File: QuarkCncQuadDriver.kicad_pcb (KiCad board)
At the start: 4 copper layers, 100 x 100 mm, 182 parts, among them J1 Screw_Terminal_01x02, J10 Screw_Terminal_01x02, J11 Screw_Terminal_01x04, J12 Screw_Terminal_01x04, J13 Screw_Terminal_01x04, J14 Conn_01x02_Male, J2 Conn_01x03_Male, J3 USB_B_Micro, J4 Screw_Terminal_01x02, J5 Screw_Terminal_01x02, J6 Conn_02x04_Odd_Even, J7 Conn_02x04_Odd_Even, J8 Conn_02x04_Odd_Even, J9 Conn_02x04_Odd_Even, Q1 WSF50P10, SW1 SW_DIP_x01, SW2 SW_DIP_x01, SW3 SW_DIP_x04, U1 StepperDriver_Conn2, U10 EL357N-G, U11 EL357N-G, U12 EL0631(TA), U13 EL357N-G, U14 EL357N-G, U15 EL0631(TA), U16 EL357N-G, U17 EL357N-G, U18 EL0631(TA), U19 StepperDriver_Conn2, U2 StepperDriver, U20 StepperDriver, U21 StepperDriver_Conn1, U22 W25Q128JVS, U23 RP2040, U24 tps54331DR, U25 LM5576, U26 SP3485EN-L/TR, U27 StepperDriver_Conn2, U28 StepperDriver, U29 StepperDriver_Conn1, U3 StepperDriver_Conn1, U4 EL357N-G, U5 EL357N-G, U6 EL0631(TA), U7 StepperDriver_Conn2, U8 StepperDriver, U9 StepperDriver_Conn1, Y1 X322512MSB4SI

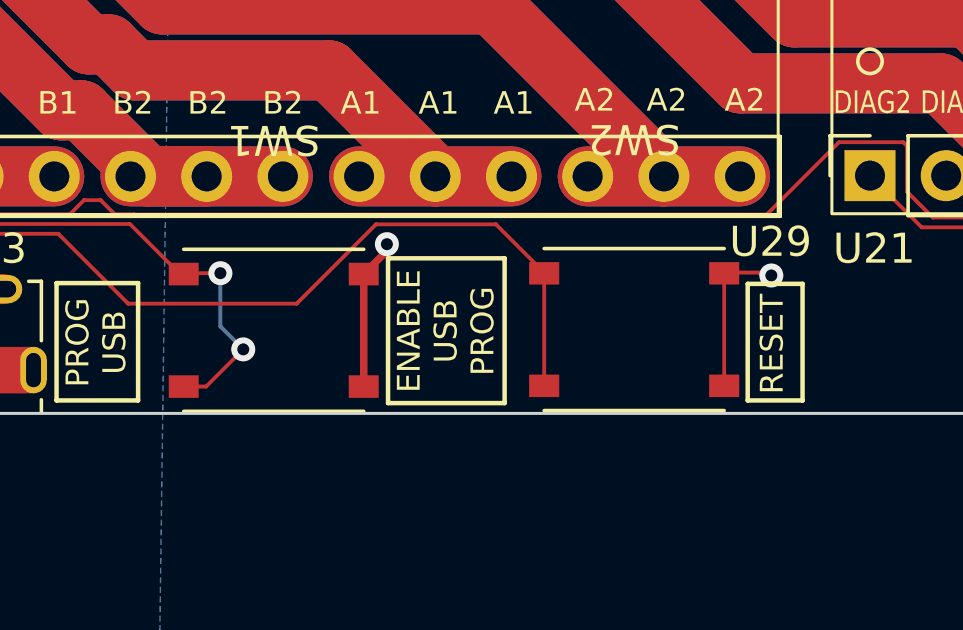
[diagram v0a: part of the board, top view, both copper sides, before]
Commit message: Fixed reset/boot button footprint
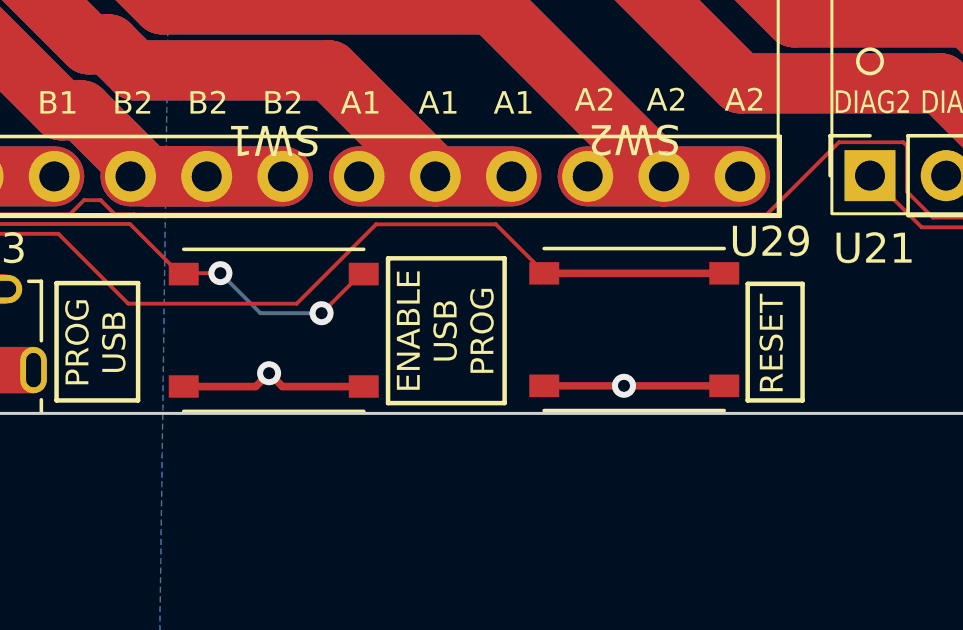
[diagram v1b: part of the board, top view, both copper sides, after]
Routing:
- net /RP2040 Microcontroller/RUN: track 141.0 -> 143.3 mm
- net GND: track 89.4 -> 91.3 mm
- net /RP2040 Microcontroller/~{USB_BOOT}: track 89.0 -> 89.6 mm

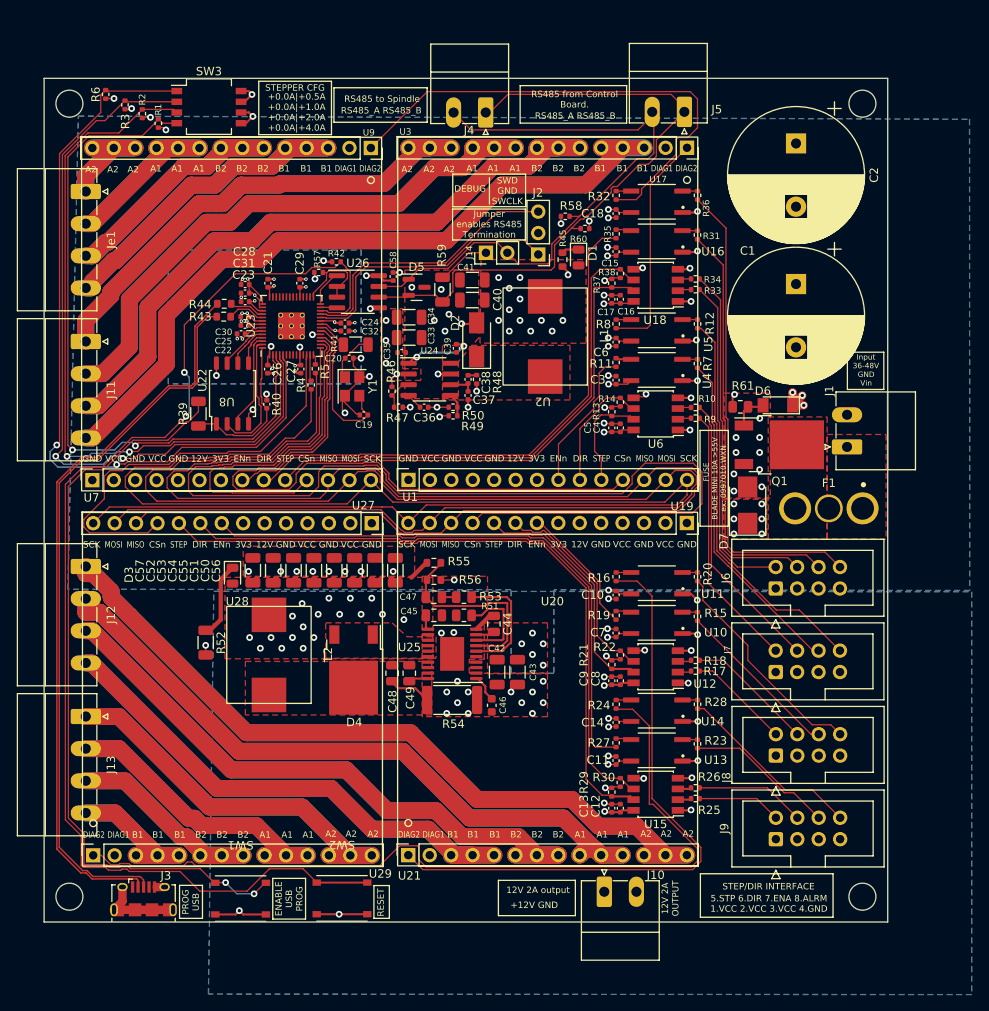
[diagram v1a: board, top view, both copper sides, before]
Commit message: Keyed stepper drivers. Larger input connector
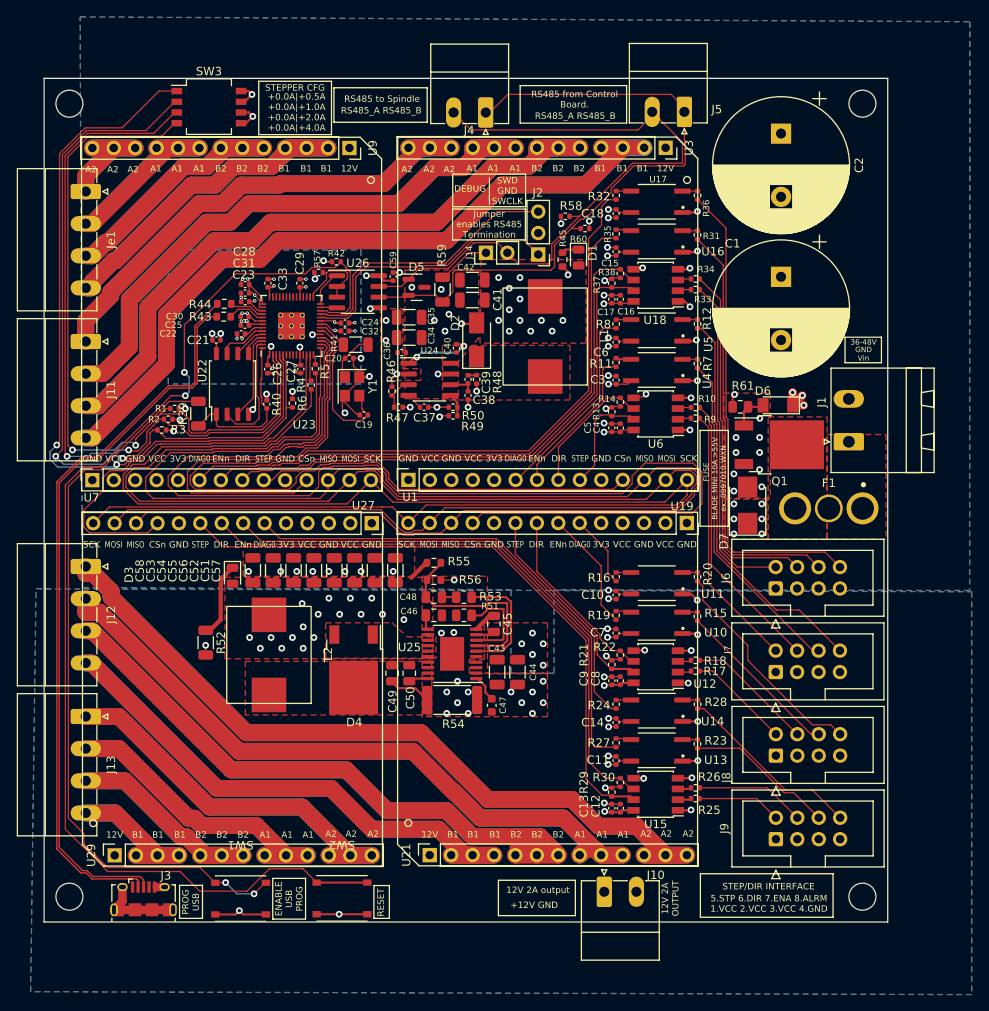
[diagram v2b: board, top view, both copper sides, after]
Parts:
- added C33: 100n 50V, Capacitor_SMD:C_0402_1005Metric, F.Cu at (63.9, 55.4)
- J1: footprint Connector_Phoenix_MC:PhoenixContact_MC_1,5_2-G-3.81_1x02_P3.81mm_Horizontal -> Connector_Phoenix_MSTB:PhoenixContact_MSTBA_2,5_2-G-5,08_1x02_P5.08mm_Horizontal
- U2, U20, U28, U8: footprint QuarkCncQuadDriver:StepperDriverV2 -> QuarkCncQuadDriver:StepperDriverV3
- U21, U29, U3, U9: footprint Connector_PinSocket_2.54mm:PinSocket_1x14_P2.54mm_Vertical -> Connector_PinSocket_2.54mm:PinSocket_1x13_P2.54mm_Vertical
- moved R6 42.8 mm to (66.8, 69.6), turned to -90 degrees
- moved R3 38.8 mm to (51.3, 72.8), turned to 180 degrees
- moved R2 36.3 mm to (52.1, 71.5), turned to 180 degrees
- moved R1 33.9 mm to (52.8, 70.2), turned to 180 degrees
- moved C21 9.08 mm to (57.8, 62.1), turned to 0 degrees
- moved U9 2.54 mm to (73.6, 39.3)
- moved U29 2.54 mm to (45.7, 123.2)
- moved U3 2.54 mm to (111.0, 39.3)
- moved U21 2.54 mm to (83.1, 123.2)
- moved C2 2.13 mm to (124.7, 37.6)
- moved C1 1.98 mm to (124.7, 54.6)
- moved U22 1.14 mm to (59.7, 67.3)
- moved J1 0.64 mm to (132.7, 74.2)
- renumbered C33 to C34, C34 to C35, C35 to C36, C36 to C37, C37 to C38, C38 to C39, C39 to C40, C40 to C41, C41 to C42, C42 to C43, C43 to C44, C44 to C45, C45 to C46, C46 to C47, C47 to C48, C48 to C49, C49 to C50, C50 to C51, C51 to C52, C52 to C53, C53 to C54, C54 to C55, C55 to C56, C56 to C57, C57 to C58, C58 to C59
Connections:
- U1 pad 10: /STEPPER_Y_STEP -> GND
- U1 pad 5: GND -> +3V3
- U1 pad 6: +12V -> /STEPPER_Y_DIAG0
- U1 pad 7: +3V3 -> /STEPPER_Y_ENn
- U1 pad 8: /STEPPER_Y_ENn -> /STEPPER_Y_DIR
- U1 pad 9: /STEPPER_Y_DIR -> /STEPPER_Y_STEP
- U19 pad 10: /STEPPER_Z_STEP -> GND
- U19 pad 5: GND -> +3V3
- U19 pad 6: +12V -> /STEPPER_Z_DIAG0
- U19 pad 7: +3V3 -> /STEPPER_Z_ENn
- U19 pad 8: /STEPPER_Z_ENn -> /STEPPER_Z_DIR
- U19 pad 9: /STEPPER_Z_DIR -> /STEPPER_Z_STEP
- U21 pad 1: /STEPPER_Z_DIAG0 -> +12V
- U21 pad 11: /STEPPER DRIVER Z/STEPPER_COIL_A1 -> /STEPPER DRIVER Z/STEPPER_COIL_A2
- U21 pad 2: /STEPPER DRIVER Z/STEPPER_DIAG1 -> /STEPPER DRIVER Z/STEPPER_COIL_B1
- U21 pad 5: /STEPPER DRIVER Z/STEPPER_COIL_B1 -> /STEPPER DRIVER Z/STEPPER_COIL_B2
- U21 pad 8: /STEPPER DRIVER Z/STEPPER_COIL_B2 -> /STEPPER DRIVER Z/STEPPER_COIL_A1
- U27 pad 10: /STEPPER_A_STEP -> GND
- U27 pad 5: GND -> +3V3
- U27 pad 6: +12V -> /STEPPER_A_DIAG0
- U27 pad 7: +3V3 -> /STEPPER_A_ENn
- U27 pad 8: /STEPPER_A_ENn -> /STEPPER_A_DIR
- U27 pad 9: /STEPPER_A_DIR -> /STEPPER_A_STEP
- U29 pad 1: /STEPPER_A_DIAG0 -> +12V
- U29 pad 11: /STEPPER DRIVER A/STEPPER_COIL_A1 -> /STEPPER DRIVER A/STEPPER_COIL_A2
- U29 pad 2: /STEPPER DRIVER A/STEPPER_DIAG1 -> /STEPPER DRIVER A/STEPPER_COIL_B1
- U29 pad 5: /STEPPER DRIVER A/STEPPER_COIL_B1 -> /STEPPER DRIVER A/STEPPER_COIL_B2
- U29 pad 8: /STEPPER DRIVER A/STEPPER_COIL_B2 -> /STEPPER DRIVER A/STEPPER_COIL_A1
- U3 pad 1: /STEPPER_Y_DIAG0 -> +12V
- U3 pad 11: /STEPPER DRIVER Y/STEPPER_COIL_A1 -> /STEPPER DRIVER Y/STEPPER_COIL_A2
- U3 pad 2: /STEPPER DRIVER Y/STEPPER_DIAG1 -> /STEPPER DRIVER Y/STEPPER_COIL_B1
- U3 pad 5: /STEPPER DRIVER Y/STEPPER_COIL_B1 -> /STEPPER DRIVER Y/STEPPER_COIL_B2
- U3 pad 8: /STEPPER DRIVER Y/STEPPER_COIL_B2 -> /STEPPER DRIVER Y/STEPPER_COIL_A1
- U7 pad 10: /STEPPER_X_STEP -> GND
- U7 pad 5: GND -> +3V3
- U7 pad 6: +12V -> /STEPPER_X_DIAG0
- U7 pad 7: +3V3 -> /STEPPER_X_ENn
- U7 pad 8: /STEPPER_X_ENn -> /STEPPER_X_DIR
- U7 pad 9: /STEPPER_X_DIR -> /STEPPER_X_STEP
- U9 pad 1: /STEPPER_X_DIAG0 -> +12V
- U9 pad 11: /STEPPER DRIVER X/STEPPER_COIL_A1 -> /STEPPER DRIVER X/STEPPER_COIL_A2
- U9 pad 2: /STEPPER DRIVER X/STEPPER_DIAG1 -> /STEPPER DRIVER X/STEPPER_COIL_B1
- U9 pad 5: /STEPPER DRIVER X/STEPPER_COIL_B1 -> /STEPPER DRIVER X/STEPPER_COIL_B2
- U9 pad 8: /STEPPER DRIVER X/STEPPER_COIL_B2 -> /STEPPER DRIVER X/STEPPER_COIL_A1
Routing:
- net /STEPPER_Z_DIAG0: track 74.6 -> 8.67 mm
- net +12V: track 90.9 -> 26.5 mm, vias 22 -> 20
- net /STEPPER_A_DIAG0: track 99.2 -> 54.6 mm
- net /STEPPER_X_DIAG0: track 59.8 -> 75.1 mm
- net /STEPPER_Y_CSn: track 77.7 -> 87.5 mm
- net /STEPPER_A_ENn: track 68.9 -> 62.5 mm
- net /STEPPER_A_STEP: track 80.7 -> 74.4 mm
- net /STEPPER_A_DIR: track 76.4 -> 70.1 mm
- net /STEPPER DRIVER Z/STEPPER_COIL_B2: track 144.2 -> 150.0 mm
- net /RS485/RS485_B: track 74.6 -> 80.4 mm
- net /STEPPER_X_CSn: track 41.9 -> 47.3 mm
- net /STEPPER_MISO: track 173.4 -> 178.8 mm
- net /STEPPER_MOSI: track 176.0 -> 180.7 mm
- net /STEPPER_Z_CSn: track 131.1 -> 135.4 mm
- net /RP2040 Microcontroller/GPIO0: track 83.6 -> 87.8 mm
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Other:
- board text added: "36-48V"
- board text removed: "Input 36-48V"
